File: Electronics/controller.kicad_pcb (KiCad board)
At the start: 2 copper layers, 100 x 75 mm, 82 parts, among them J501 Conn_01x06_Female, J502 Motor Con, J503 Conn_01x05_Female, Q201 IRLZ44N, Q202 IRLIZ44N, Q203 IRLZ44N, Q204 IRLIZ44N, Q205 IRLZ44N, Q206 IRLIZ44N, U1 R-78C15-1.0, U201 74LS08, U202 IR2101, U203 IR2101, U204 IR2101, U301 74HC86, U402 R-78E3.3-1.0

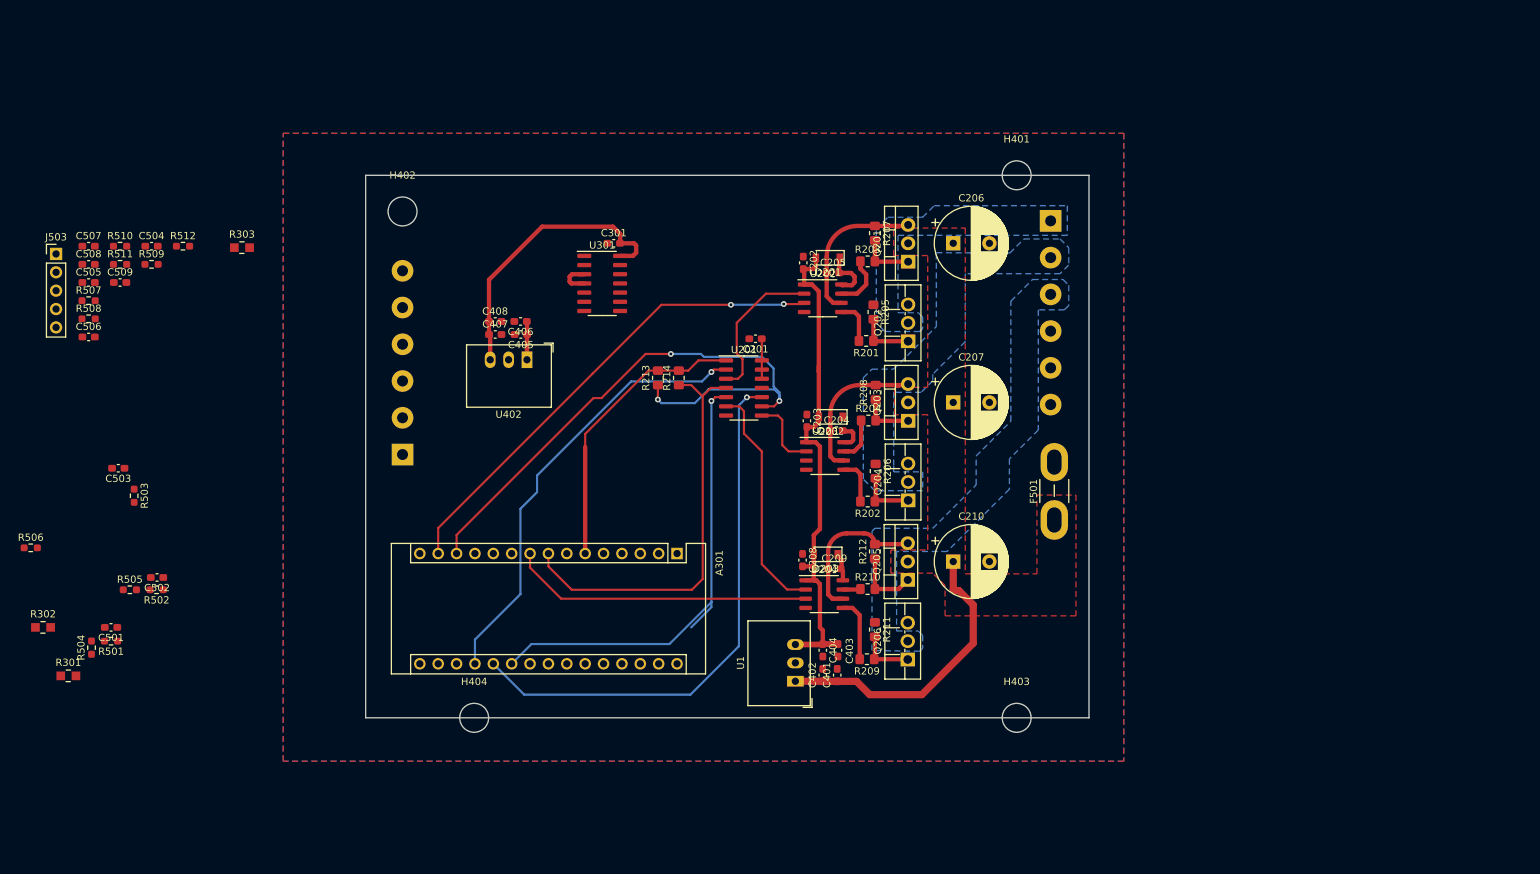
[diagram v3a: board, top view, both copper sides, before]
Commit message: Added Current sensor finalized layout version 0.1
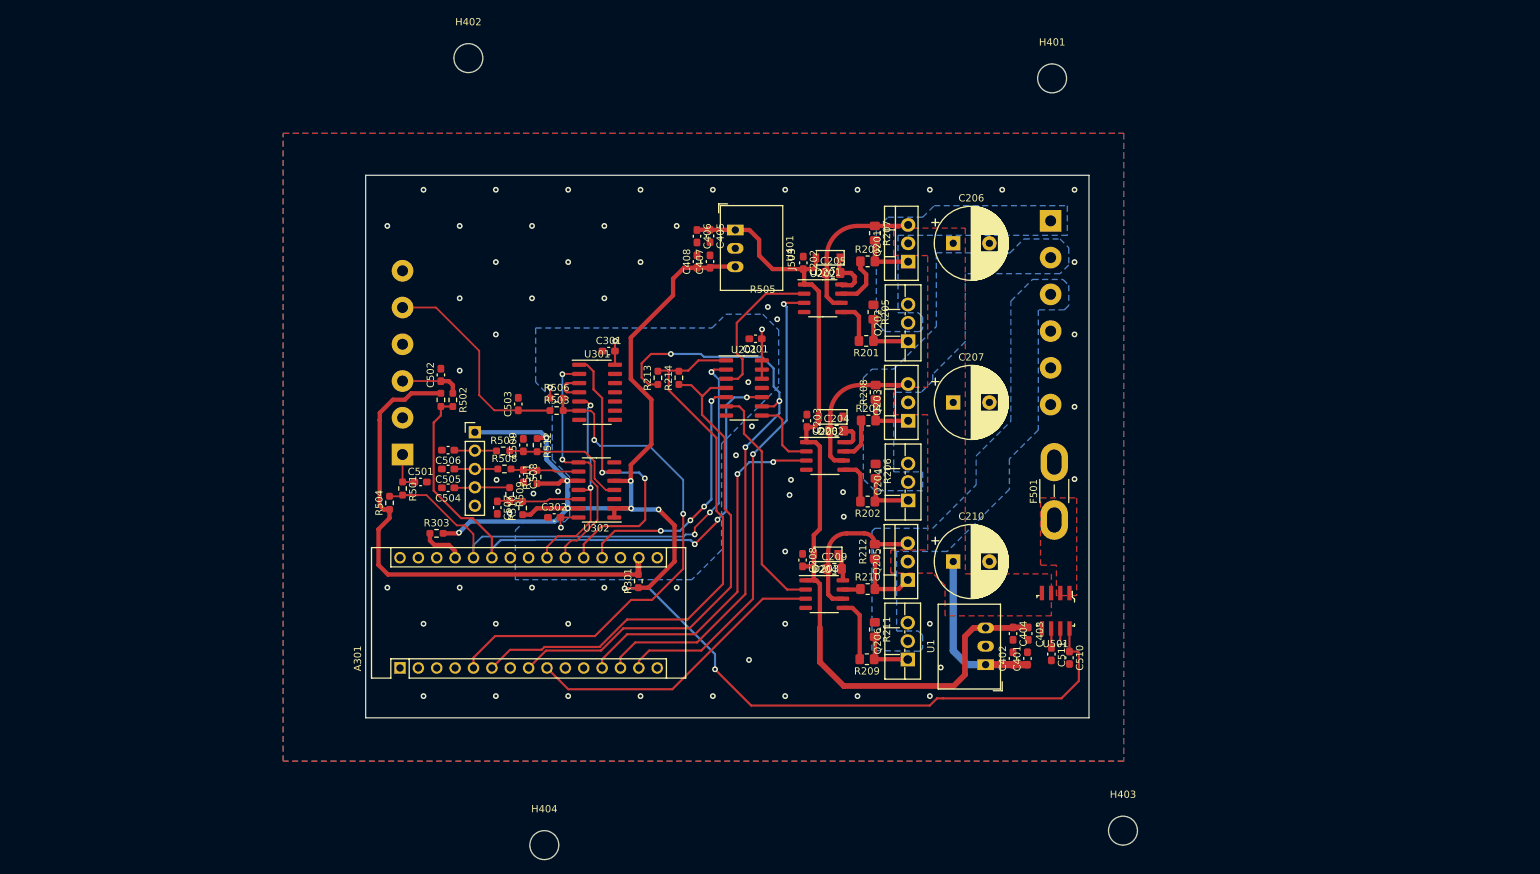
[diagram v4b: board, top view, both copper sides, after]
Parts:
- removed R302: 0r, digikey-footprints:0805
- removed U402: R-78E3.3-1.0, Converter_DCDC:Converter_DCDC_RECOM_R-78E-0.5_THT
- added C302: 100n, Capacitor_SMD:C_0603_1608Metric_Pad1.08x0.95mm_HandSolder, F.Cu at (103.1, 100.3)
- added C510: 100n, Capacitor_SMD:C_0603_1608Metric_Pad1.08x0.95mm_HandSolder, F.Cu at (174.3, 119.7)
- added C511: 100n, Capacitor_SMD:C_0603_1608Metric_Pad1.08x0.95mm_HandSolder, F.Cu at (171.8, 119.2)
- added U302: 74AHC08, Package_SO:SO-14_3.9x8.65mm_P1.27mm, F.Cu at (108.9, 96.5)
- added U401: R-78C5.0-1.0, Converter_DCDC:Converter_DCDC_RECOM_R-78E-0.5_THT, F.Cu at (128.1, 60.6)
- added U501: ACS712ELCTR-20A-T_NRND, digikey-footprints:SOIC-8_W3.9mm, F.Cu at (172.4, 113.2)
- C204, C205, C209: footprint Capacitor_SMD:C_0603_1608Metric_Pad1.08x0.95mm_HandSolder -> Resistor_SMD:R_0805_2012Metric_Pad1.20x1.40mm_HandSolder
- R213, R214: footprint Resistor_SMD:R_0805_2012Metric_Pad1.20x1.40mm_HandSolder -> Resistor_SMD:R_0603_1608Metric_Pad0.98x0.95mm_HandSolder
- R301, R303: value 0r -> 0; footprint digikey-footprints:0805 -> Resistor_SMD:R_0603_1608Metric_Pad0.98x0.95mm_HandSolder
- U201: value 74LS08 -> 74AHC08
- moved R301 79.9 mm to (114.7, 109.1), turned to 90 degrees
- moved R506 75.6 mm to (103.4, 83.8)
- moved C507 67.1 mm to (95.2, 98.9), turned to -90 degrees
- moved C508 66.9 mm to (98.8, 94.6), turned to -90 degrees
- moved R510 66.4 mm to (98.7, 99.0), turned to 90 degrees
- moved R511 64.7 mm to (100.7, 94.7), turned to 90 degrees
- moved J503 62.9 mm to (92.1, 88.5)
- moved R508 61.1 mm to (96.2, 93.6)
- moved R507 61.0 mm to (96.0, 91.1)
- moved C509 60.1 mm to (98.8, 90.3), turned to 90 degrees
- moved R503 59.6 mm to (103.4, 85.5), turned to 0 degrees
- moved R509 58.8 mm to (96.9, 97.1), turned to -90 degrees
- moved R512 56.1 mm to (100.7, 90.3), turned to -90 degrees
- moved C503 56.0 mm to (98.1, 84.6), turned to 90 degrees
- moved C505 56.0 mm to (88.4, 93.6), turned to 180 degrees
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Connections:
- A301 pad 10: /MCU/HALL A -> unconnected-(A301-Pad10)
- A301 pad 11: /MCU/HALL B -> unconnected-(A301-Pad11)
- A301 pad 17: Net-(A301-Pad17) -> +3V3
- A301 pad 19: /Connectors/Limit 1 -> /Hbridge/C LIMIT
- A301 pad 20: /Connectors/Limit 2 -> /MCU/HALL A OUT
- A301 pad 21: /Hbridge/C LIMIT -> /MCU/HALL B OUT
- A301 pad 22: unconnected-(A301-Pad22) -> /MCU/HALL C OUT
- A301 pad 25: unconnected-(A301-Pad25) -> /Connectors/Limit 2
- A301 pad 26: unconnected-(A301-Pad26) -> /Connectors/Limit 1
- A301 pad 30: Net-(A301-Pad30) -> unconnected-(A301-Pad30)
- A301 pad 7: /MCU/HALL C -> unconnected-(A301-Pad7)
- C201 pad 1: VDD -> +3V3
- C301 pad 2: VDD -> +3V3
- F501 pad 1: Vdrive -> /Connectors/PWR IN
- R301 pad 1: Net-(A301-Pad30) -> VDD
- R301 pad 2: VCC -> +3V3
- R504 pad 1: VDD -> +3V3
- R505 pad 1: VDD -> +3V3
- R506 pad 1: VDD -> +3V3
- U201 pad 12: VDD -> +3V3
- U201 pad 13: VDD -> +3V3
- U201 pad 14: VDD -> +3V3
- U301 pad 1: /MCU/HALL A -> /MCU/HALL A OUT
- U301 pad 14: VDD -> +3V3
- U301 pad 2: /MCU/HALL B -> /MCU/HALL B OUT
- U301 pad 5: /MCU/HALL C -> /MCU/HALL C OUT
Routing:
- net VDD: track 45.3 -> 216.7 mm, vias 0 -> 9
- net +3V3: track 0.00 -> 86.7 mm, vias 0 -> 4
- net /Connectors/Button: track 0.00 -> 72.2 mm, vias 0 -> 2
- net /Hbridge/LIN B: track 0.00 -> 50.4 mm, vias 0 -> 2
- net VCC: track 75.1 -> 120.3 mm
- net /MCU/HALL A OUT: track 0.00 -> 42.3 mm, vias 0 -> 2
- net /MCU/HALL B OUT: track 0.00 -> 33.9 mm, vias 0 -> 2
- net /Hbridge/C LIMIT: track 65.8 -> 35.4 mm, vias 1 -> 4
- net Net-(C503-Pad1): track 0.00 -> 29.9 mm
- net /MCU/HALL C OUT: track 0.00 -> 28.9 mm, vias 0 -> 2
- net /Hbridge/HIN A: track 55.0 -> 79.4 mm
- net /Connectors/Limit 2: track 75.4 -> 96.7 mm, vias 1 -> 3
- net /Connectors/HALL A: track 0.00 -> 18.1 mm
- net Vdrive: track 41.1 -> 23.4 mm
- net /Connectors/Limit 1: track 61.8 -> 76.5 mm, vias 1 -> 3
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- added copper zone on B.Cu, net +3V3
- added copper zone on F.Cu, net /Connectors/PWR IN
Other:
- board text added: "0.2000 mm / 0.0000 mm"
- board text added: "0.3000 mm"
- board text added: "1.6000 mm"
- board text added: "100.1000 mm x 75.1000 mm"
- board text added: "2"
- board text added: "BOARD CHARACTERISTICS"
- board text added: "Board Thickness:"
- board text added: "Board overall dimensions:"
- board text added: "Castellated pads:"
- board text added: "Copper Finish:"
- board text added: "Copper Layer Count:"
- board text added: "Edge card connectors:"
- board text added: "HAL lead-free"
- board text added: "Impedance Control:"
- board text added: "Min hole diameter:"
- board text added: "Min track/spacing:"
- board text added: "No"
- board text added: "Plated Board Edge:"

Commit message: Added current sensor circuitry
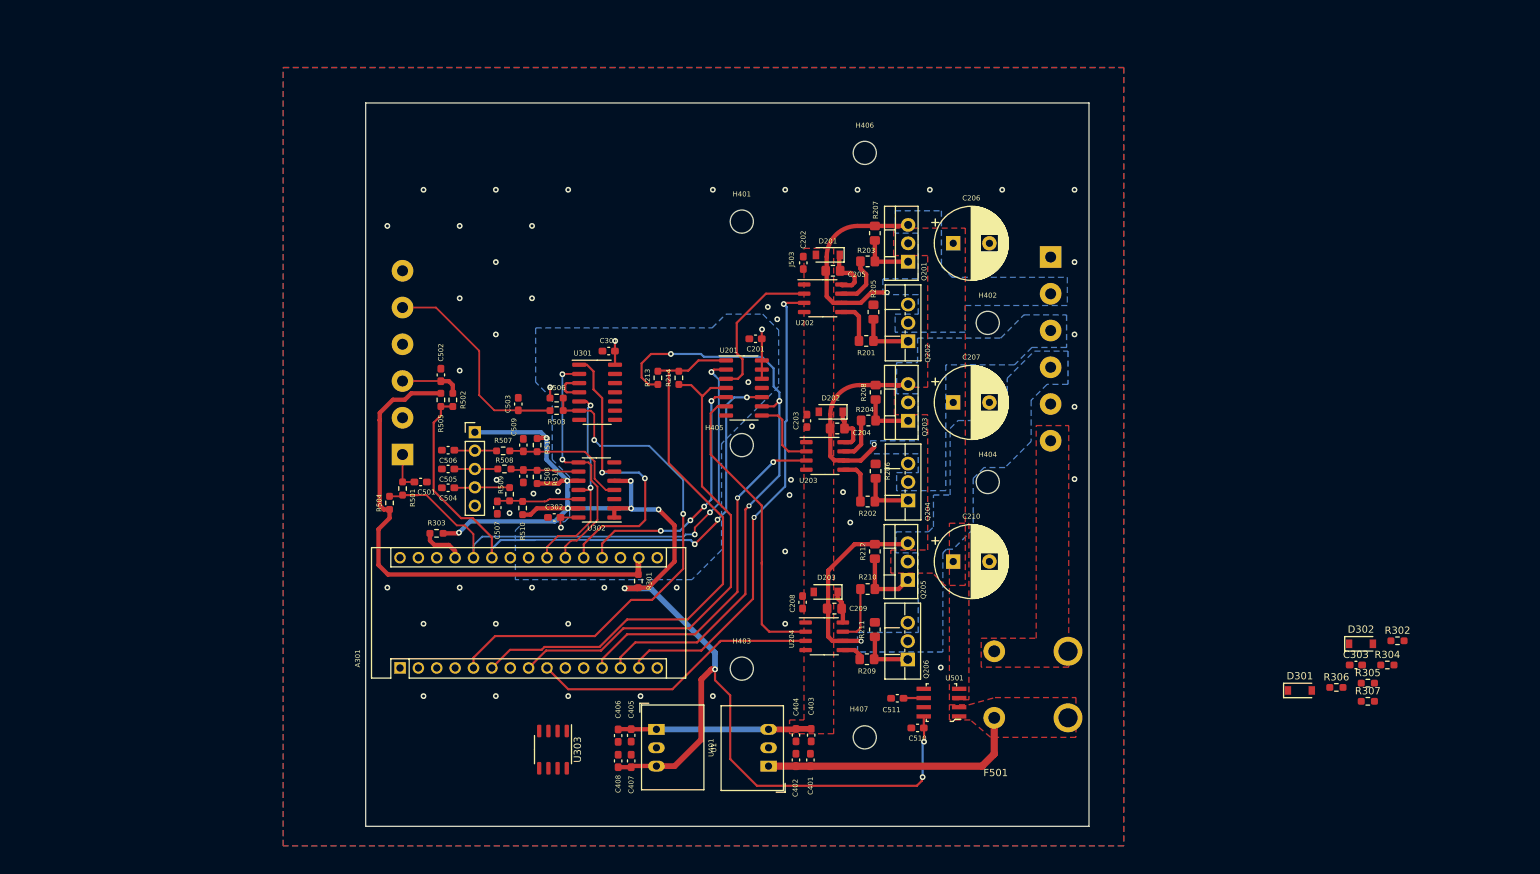
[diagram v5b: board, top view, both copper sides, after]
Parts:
- added C303: 100n, Capacitor_SMD:C_0603_1608Metric_Pad1.08x0.95mm_HandSolder, F.Cu at (213.9, 120.7)
- added D301: 1N5819, Diode_SMD:D_SOD-123, F.Cu at (206.2, 124.2)
- added D302: 1N5819, Diode_SMD:D_SOD-123, F.Cu at (214.6, 117.8)
- added H405: MountingHole, MountingHole:MountingHole_3.2mm_M3_DIN965, F.Cu at (129.0, 90.3)
- added H406: MountingHole, MountingHole:MountingHole_3.2mm_M3_DIN965, F.Cu at (146.0, 49.9)
- added H407: MountingHole, MountingHole:MountingHole_3.2mm_M3_DIN965, F.Cu at (146.0, 130.7)
- added R302: 0, Resistor_SMD:R_0603_1608Metric_Pad0.98x0.95mm_HandSolder, F.Cu at (219.7, 117.3)
- added R304: R_Small, Resistor_SMD:R_0603_1608Metric_Pad0.98x0.95mm_HandSolder, F.Cu at (218.2, 120.7)
- added R305: R_Small, Resistor_SMD:R_0603_1608Metric_Pad0.98x0.95mm_HandSolder, F.Cu at (215.6, 123.2)
- added R306: R_Small, Resistor_SMD:R_0603_1608Metric_Pad0.98x0.95mm_HandSolder, F.Cu at (211.2, 123.8)
- added R307: R_Small, Resistor_SMD:R_0603_1608Metric_Pad0.98x0.95mm_HandSolder, F.Cu at (215.6, 125.7)
- added U303: LM393, Package_SO:SO-8_3.9x4.9mm_P1.27mm, F.Cu at (102.9, 132.4)
- F501: footprint Fuse:Fuse_Blade_Mini_directSolder -> digikey-footprints:3550-2_KEYS
- H401, H402, H403, H404: footprint MountingHole:MountingHole_4mm -> MountingHole:MountingHole_3.2mm_M3_DIN965
- moved H402 80.6 mm to (163.0, 73.4)
- moved H404 79.2 mm to (163.0, 95.4)
- moved C405 69.9 mm to (113.7, 130.4)
- moved C406 69.9 mm to (111.9, 130.5)
- moved C407 69.9 mm to (113.7, 134.0)
- moved C408 69.9 mm to (111.9, 134.0)
- moved U401 69.9 mm to (117.2, 129.6)
- moved H403 57.3 mm to (129.0, 121.2)
- moved H401 47.2 mm to (129.0, 59.4)
- moved U1 33.1 mm to (132.7, 134.7)
- moved C401 33.1 mm to (138.5, 133.8)
- moved C402 33.1 mm to (136.5, 133.8)
- moved C403 33.1 mm to (138.6, 130.4)
- moved C404 33.1 mm to (136.5, 130.4)
- moved C510 23.1 mm to (153.3, 129.4), turned to 180 degrees
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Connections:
- C401 pad 1: Vdrive -> VD
- C402 pad 1: Vdrive -> VD
- F501 pad 1: /Connectors/PWR IN -> VD
- F501 pad 2: Net-(F501-Pad2) -> /Connectors/PWR IN
- J502 pad 1: /Connectors/MOTOR POS -> GND
- J502 pad 2: /Connectors/MOTOR NEG -> /Connectors/MOTOR POS
- J502 pad 3: /Connectors/MOTOR C -> /Connectors/MOTOR NEG
- J502 pad 4: unconnected-(J502-Pad4) -> /Connectors/MOTOR C
- J502 pad 5: GND -> unconnected-(J502-Pad5)
- J502 pad 6: Net-(F501-Pad2) -> /Connectors/PWR IN
- U1 pad 1: Vdrive -> VD
- U501 pad 1: /Connectors/PWR IN -> VD
- U501 pad 2: /Connectors/PWR IN -> VD
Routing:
- net VCC: track 120.3 -> 27.0 mm
- net VD: track 0.00 -> 36.9 mm
- net VDD: track 216.7 -> 187.0 mm, vias 9 -> 11
- net Vdrive: track 23.4 -> 0.00 mm
- net Net-(U201-Pad6): track 32.4 -> 41.3 mm
- net /Connectors/MOTOR POS: track 21.5 -> 28.4 mm, vias 0 -> 1
- net Net-(R210-Pad1): track 2.45 -> 8.12 mm
- net Net-(R209-Pad2): track 8.84 -> 3.20 mm
- net /Connectors/MOTOR NEG: track 20.8 -> 26.2 mm, vias 0 -> 1
- net /Connectors/MOTOR C: track 21.4 -> 26.5 mm, vias 0 -> 1
- net Net-(C204-Pad2): track 3.87 -> 6.59 mm
- net /Hbridge/LIN C: track 42.2 -> 39.7 mm
- net /Hbridge/LIN B: track 50.4 -> 48.4 mm
- net /Connectors/VIOUT: track 1.61 -> 0.00 mm
- net GND: vias 61 -> 49
- added copper zone on F.Cu, net VCC
- added copper zone on F.Cu, net VD
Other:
- board size 100 x 75 mm -> 100 x 100 mm

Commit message: Updated Design
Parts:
- removed D301, D302: 1N5819, Diode_SMD:D_SOD-123
- removed R304, R305, R306, R307: R_Small, Resistor_SMD:R_0603_1608Metric_Pad0.98x0.95mm_HandSolder
- removed U303: LM393, Package_SO:SO-8_3.9x4.9mm_P1.27mm
- added C512: 100n, Capacitor_SMD:C_0603_1608Metric_Pad1.08x0.95mm_HandSolder, F.Cu at (90.1, 128.1)
- added C513: 10n, Capacitor_SMD:C_0603_1608Metric_Pad1.08x0.95mm_HandSolder, F.Cu at (111.7, 133.3)
- added C514: 100n, Capacitor_SMD:C_0603_1608Metric_Pad1.08x0.95mm_HandSolder, F.Cu at (104.5, 128.8)
- added C515: 100n, Capacitor_SMD:C_0603_1608Metric_Pad1.08x0.95mm_HandSolder, F.Cu at (94.0, 134.6)
- added C516: 100n, Capacitor_SMD:C_0603_1608Metric_Pad1.08x0.95mm_HandSolder, F.Cu at (98.0, 124.5)
- added D501: 1N5819, Diode_SMD:D_SOD-123, F.Cu at (97.2, 126.6)
- added D502: LED, LED_SMD:LED_1206_3216Metric_Pad1.42x1.75mm_HandSolder, F.Cu at (82.7, 131.7)
- added H408: MountingHole, MountingHole:MountingHole_3.2mm_M3_DIN965, F.Cu at (82.0, 48.0)
- added H409: MountingHole, MountingHole:MountingHole_3.2mm_M3_DIN965, F.Cu at (172.0, 48.0)
- added H410: MountingHole, MountingHole:MountingHole_3.2mm_M3_DIN965, F.Cu at (172.0, 138.0)
- added H411: MountingHole, MountingHole:MountingHole_3.2mm_M3_DIN965, F.Cu at (82.0, 138.0)
- added J301: UART, Connector_PinHeader_2.54mm:PinHeader_1x03_P2.54mm_Vertical, F.Cu at (89.2, 116.2)
- added Q501: BC817, Package_TO_SOT_SMD:SOT-23, F.Cu at (100.0, 135.9)
- added R513: 11k, Resistor_SMD:R_0603_1608Metric_Pad0.98x0.95mm_HandSolder, F.Cu at (111.8, 134.9)
- added R514: 11k, Resistor_SMD:R_0603_1608Metric_Pad0.98x0.95mm_HandSolder, F.Cu at (109.1, 133.7)
- added R515: 10k, Resistor_SMD:R_0603_1608Metric_Pad0.98x0.95mm_HandSolder, F.Cu at (102.7, 130.6)
- added R516: 0, Resistor_SMD:R_0603_1608Metric_Pad0.98x0.95mm_HandSolder, F.Cu at (102.7, 132.2)
- added R517: 11k, Resistor_SMD:R_0603_1608Metric_Pad0.98x0.95mm_HandSolder, F.Cu at (93.9, 125.7)
- added R518: 1k, LED_SMD:LED_0603_1608Metric_Pad1.05x0.95mm_HandSolder, F.Cu at (89.7, 133.0)
- added R519: 11k, Resistor_SMD:R_0603_1608Metric_Pad0.98x0.95mm_HandSolder, F.Cu at (94.1, 136.7)
- added R520: 100k, Resistor_SMD:R_0603_1608Metric_Pad0.98x0.95mm_HandSolder, F.Cu at (97.0, 135.8)
- added RV501: 50k, Potentiometer_SMD:Potentiometer_Vishay_TS53YJ_Vertical, F.Cu at (103.7, 124.5)
- added S501: B3U-1000P, digikey-footprints:Switch_Tactile_SMD_B3U-1000P, F.Cu at (104.2, 136.9)
- added TP501: GND, TestPoint:TestPoint_Pad_1.5x1.5mm, F.Cu at (108.0, 136.7)
- added TP502: Current Out Att, TestPoint:TestPoint_Pad_D1.0mm, F.Cu at (110.8, 137.0)
- added TP503: Current Out, TestPoint:TestPoint_Pad_D1.0mm, F.Cu at (158.8, 133.0)
- added TP504: Current Out AMP, TestPoint:TestPoint_Pad_D1.0mm, F.Cu at (103.6, 134.1)
- added TP505: GND, TestPoint:TestPoint_Pad_1.5x1.5mm, F.Cu at (158.3, 130.3)
- added TP506: Current Limit, TestPoint:TestPoint_Pad_D1.0mm, F.Cu at (98.9, 122.6)
- added TP507: GND, TestPoint:TestPoint_Pad_1.5x1.5mm, F.Cu at (92.9, 120.7)
- added U502: LM393, Package_SO:SO-8_3.9x4.9mm_P1.27mm, F.Cu at (95.7, 131.1)
- added U503: 74AHC08, Package_SO:SO-14_3.9x8.65mm_P1.27mm, F.Cu at (84.6, 126.5)
- added U504: MCP6001-OT, Package_TO_SOT_SMD:SOT-23-5, F.Cu at (106.5, 131.8)
- C401, C403, C405: value C -> 4u7; footprint Capacitor_SMD:C_0603_1608Metric_Pad1.08x0.95mm_HandSolder -> Resistor_SMD:R_0805_2012Metric_Pad1.20x1.40mm_HandSolder
- C402, C404, C406, C407: value C -> 100n
- C408: value C -> 10u; footprint Capacitor_SMD:C_0603_1608Metric_Pad1.08x0.95mm_HandSolder -> Resistor_SMD:R_0805_2012Metric_Pad1.20x1.40mm_HandSolder
- J501: value Conn_01x06_Female -> Switches
- J503: value Conn_01x05_Female -> Hall Sensor
- U501: value ACS712ELCTR-20A-T_NRND -> ‎ACHS-7124-000E‎; footprint digikey-footprints:SOIC-8_W3.9mm -> Package_SO:SO-8_3.9x4.9mm_P1.27mm
- moved R302 106.6 mm to (115.6, 94.2)
- moved C303 102.3 mm to (115.6, 92.4), turned to 180 degrees
- moved R503 14.1 mm to (102.6, 71.4)
- moved R506 14.1 mm to (102.6, 69.7)
- moved C301 14.1 mm to (109.8, 63.2)
- moved C503 14.1 mm to (97.3, 70.5)
- moved U301 14.1 mm to (108.2, 68.9)
- moved R502 9.69 mm to (88.2, 74.4), turned to 0 degrees
- moved R301 9.63 mm to (116.3, 99.6), turned to 0 degrees
- moved A301 9.31 mm to (84.2, 112.1)
- moved C502 8.76 mm to (87.3, 71.8)
- moved C504 8.75 mm to (87.8, 87.5)
- moved C501 8.73 mm to (84.2, 86.7)
- moved R509 8.73 mm to (96.5, 88.4)
- moved R511 8.73 mm to (100.3, 86.0)
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- renumbered U1 to U402
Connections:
- A301 pad 1: unconnected-(A301-Pad1) -> /MCU/TX
- A301 pad 10: unconnected-(A301-Pad10) -> /Connectors/Limit 1
- A301 pad 11: unconnected-(A301-Pad11) -> /Connectors/Limit 2
- A301 pad 15: unconnected-(A301-Pad15) -> /Hbridge/C LIMIT
- A301 pad 18: unconnected-(A301-Pad18) -> Net-(A301-Pad18)
- A301 pad 19: /Hbridge/C LIMIT -> unconnected-(A301-Pad19)
- A301 pad 2: unconnected-(A301-Pad2) -> /MCU/RX
- A301 pad 25: /Connectors/Limit 2 -> /Connectors/VIOUT
- A301 pad 26: /Connectors/Limit 1 -> unconnected-(A301-Pad26)
- A301 pad 7: unconnected-(A301-Pad7) -> /Connectors/Latch Reset
- C303 pad 2: VDD -> Net-(A301-Pad18)
- C511 pad 1: Net-(C511-Pad1) -> GND
- C511 pad 2: GND -> Net-(U501-Pad6)
- R302 pad 1: Net-(R302-Pad1) -> Net-(A301-Pad18)
- R302 pad 2: /MCU/V IOUT -> +3V3
- R501 pad 2: /Connectors/Limit 1 -> /Connectors/LIMIT 1
- R502 pad 2: /Connectors/Limit 2 -> /Connectors/LIMIT 2
- R504 pad 1: +3V3 -> VDD
- R504 pad 2: /Connectors/Limit 1 -> /Connectors/LIMIT 1
- R505 pad 1: +3V3 -> VDD
- R505 pad 2: /Connectors/Limit 2 -> /Connectors/LIMIT 2
- U302 pad 1: VDD -> unconnected-(U302-Pad1)
- U302 pad 2: VDD -> unconnected-(U302-Pad2)
- U501 pad 6: Net-(C511-Pad1) -> Net-(U501-Pad6)
- U501 pad 7: /Connectors/VIOUT -> Net-(U501-Pad7)
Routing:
- net VDD: track 187.0 -> 309.0 mm, vias 11 -> 6
- net Net-(U501-Pad7): track 0.00 -> 60.8 mm, vias 0 -> 2
- net /Connectors/LIMIT 2: track 0.00 -> 50.4 mm, vias 0 -> 2
- net /Connectors/LIMIT 1: track 0.00 -> 38.2 mm, vias 0 -> 2
- net /Connectors/VIOUT: track 0.00 -> 37.9 mm, vias 0 -> 1
- net Net-(D501-Pad1): track 0.00 -> 35.4 mm
- net /Connectors/Latch Reset: track 0.00 -> 30.0 mm, vias 0 -> 1
- net /Hbridge/HIN B: track 82.8 -> 66.8 mm
- net /Hbridge/HIN A: track 79.4 -> 63.5 mm
- net /Hbridge/HIN C: track 68.3 -> 52.7 mm
- net /Connectors/Limit 2: track 96.7 -> 81.4 mm, vias 3 -> 1
- net /Hbridge/LIN B: track 48.4 -> 34.0 mm
- net Net-(R515-Pad1): track 0.00 -> 14.3 mm
- net Net-(C516-Pad2): track 0.00 -> 14.2 mm
- net /Hbridge/LIN A: track 66.0 -> 52.1 mm
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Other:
- board text added: "GND BTN LIM 2 GND LIM 1 GND"
- board text added: "GND Motor A Motor B Motor C NC Power MAX 40V"
- board text added: "TX G RX"
